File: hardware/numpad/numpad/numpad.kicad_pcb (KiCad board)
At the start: 4 copper layers, 123.8 x 142.9 mm, 57 parts, among them SW1 ROT_SKYLOONG_HS

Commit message: LEDs attached to switches
LEDs are assigned to the switches now
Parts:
- moved LED6 139.1 mm to (133.4, 71.1)
- moved LED5 136.4 mm to (133.5, 42.9)
- moved LED14 133.1 mm to (114.1, 91.1)
- moved LED8 120.0 mm to (95.3, 71.6)
- moved LED7 119.6 mm to (114.4, 71.9)
- moved LED4 117.6 mm to (114.4, 43.1)
- moved LED13 117.3 mm to (95.3, 90.6)
- moved LED12 103.0 mm to (76.3, 91.1)
- moved LED9 100.9 mm to (76.3, 71.8)
- moved LED3 99.4 mm to (95.4, 42.9)
- moved LED11 83.3 mm to (47.7, 90.8)
- moved LED2 81.7 mm to (76.3, 42.9)
- moved LED10 74.1 mm to (47.7, 71.8)
- moved LED1 56.6 mm to (47.6, 43.2)
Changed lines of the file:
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@@
 	(footprint "PCM_marbastlib-mx:LED_MX_6028R"
 		(layer "B.Cu")
-		(at -11.59 27.25 180)
+		(at 47.694 71.767 180)
 		(descr "Add-on for regular MX-footprints with 6028 reverse mount LED")
 		(tags "cherry MX 6028 rearmount rear mount led rgb backlight")
@@
 	(footprint "PCM_marbastlib-mx:LED_MX_6028R"
 		(layer "B.Cu")
-		(at -11.59 37.35 180)
+		(at 76.269 91.071 180)
 		(descr "Add-on for regular MX-footprints with 6028 reverse mount LED")
 		(tags "cherry MX 6028 rearmount rear mount led rgb backlight")
@@
 	(footprint "PCM_marbastlib-mx:LED_MX_6028R"
 		(layer "B.Cu")
-		(at -11.59 17.15 180)
+		(at 95.319 71.64 180)
 		(descr "Add-on for regular MX-footprints with 6028 reverse mount LED")
 		(tags "cherry MX 6028 rearmount rear mount led rgb backlight")
@@
 	(footprint "PCM_marbastlib-mx:LED_MX_6028R"
 		(layer "B.Cu")
-		(at -11.59 47.45 180)
+		(at 114.115 91.071 180)
 		(descr "Add-on for regular MX-footprints with 6028 reverse mount LED")
 		(tags "cherry MX 6028 rearmount rear mount led rgb backlight")
@@
 	(footprint "PCM_marbastlib-mx:LED_MX_6028R"
 		(layer "B.Cu")
-		(at -2.725 22.2 180)
+		(at 76.269 42.938 180)
 		(descr "Add-on for regular MX-footprints with 6028 reverse mount LED")
 		(tags "cherry MX 6028 rearmount rear mount led rgb backlight")
@@
 	(footprint "PCM_marbastlib-mx:LED_MX_6028R"
 		(layer "B.Cu")
-		(at -11.59 22.2 180)
+		(at 76.269 71.767 180)
 		(descr "Add-on for regular MX-footprints with 6028 reverse mount LED")
 		(tags "cherry MX 6028 rearmount rear mount led rgb backlight")
@@
 	(footprint "PCM_marbastlib-mx:LED_MX_6028R"
 		(layer "B.Cu")
-		(at -2.725 37.35 180)
+		(at 133.546 42.938 180)
 		(descr "Add-on for regular MX-footprints with 6028 reverse mount LED")
 		(tags "cherry MX 6028 rearmount rear mount led rgb backlight")
@@
 	(footprint "PCM_marbastlib-mx:LED_MX_6028R"
 		(layer "B.Cu")
-		(at -2.725 17.15 180)
+		(at 47.567 43.192 180)
 		(descr "Add-on for regular MX-footprints with 6028 reverse mount LED")
 		(tags "cherry MX 6028 rearmount rear mount led rgb backlight")
@@
 	(footprint "PCM_marbastlib-mx:LED_MX_6028R"
 		(layer "B.Cu")
-		(at -11.59 42.4 180)
+		(at 95.319 90.563 180)
 		(descr "Add-on for regular MX-footprints with 6028 reverse mount LED")
 		(tags "cherry MX 6028 rearmount rear mount led rgb backlight")
@@
 	(footprint "PCM_marbastlib-mx:LED_MX_6028R"
 		(layer "B.Cu")
-		(at -2.725 47.45 180)
+		(at 114.369 71.894 180)
 		(descr "Add-on for regular MX-footprints with 6028 reverse mount LED")
 		(tags "cherry MX 6028 rearmount rear mount led rgb backlight")
@@
 	(footprint "PCM_marbastlib-mx:LED_MX_6028R"
 		(layer "B.Cu")
-		(at -2.725 32.3 180)
+		(at 114.369 43.065 180)
 		(descr "Add-on for regular MX-footprints with 6028 reverse mount LED")
 		(tags "cherry MX 6028 rearmount rear mount led rgb backlight")
@@
 	(footprint "PCM_marbastlib-mx:LED_MX_6028R"
 		(layer "B.Cu")
-		(at -2.725 27.25 180)
+		(at 95.446 42.938 180)
 		(descr "Add-on for regular MX-footprints with 6028 reverse mount LED")
 		(tags "cherry MX 6028 rearmount rear mount led rgb backlight")
@@
 	(footprint "PCM_marbastlib-mx:LED_MX_6028R"
 		(layer "B.Cu")
-		(at -2.725 42.4 180)
+		(at 133.419 71.132 180)
 		(descr "Add-on for regular MX-footprints with 6028 reverse mount LED")
 		(tags "cherry MX 6028 rearmount rear mount led rgb backlight")
@@
 	(footprint "PCM_marbastlib-mx:LED_MX_6028R"
 		(layer "B.Cu")
-		(at -11.59 32.3 180)
+		(at 47.694 90.817 180)
 		(descr "Add-on for regular MX-footprints with 6028 reverse mount LED")
 		(tags "cherry MX 6028 rearmount rear mount led rgb backlight")

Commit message: led
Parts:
- moved LED27 178.0 mm to (142.8, -3.03)
- moved LED20 157.9 mm to (134.0, -3.03)
- moved LED25 154.2 mm to (142.8, 7.07)
- moved LED21 151.1 mm to (134.0, -8.08), turned to 0 degrees
- moved LED26 148.0 mm to (142.8, 2.02)
- moved LED19 137.7 mm to (134.0, 2.02)
- moved LED24 134.0 mm to (142.8, 12.1)
- moved LED23 120.9 mm to (142.8, 17.2)
- moved LED18 117.4 mm to (134.0, 7.07)
- moved LED11 114.0 mm to (125.1, 7.07), turned to 0 degrees
- moved LED22 109.9 mm to (142.8, 22.2)
- moved LED17 104.6 mm to (134.0, 12.1)
- moved LED12 101.6 mm to (125.1, 2.02), turned to 0 degrees
- moved LED14 99.8 mm to (125.1, -8.08), turned to 0 degrees
- moved LED13 98.2 mm to (125.1, -3.03), turned to 0 degrees
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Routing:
- net Net-(LED16-DOUT): track 48.2 -> 0.00 mm
- net Net-(LED1-DOUT): track 0.00 -> 43.3 mm
- net Net-(LED24-DOUT): track 39.1 -> 0.00 mm
- net Net-(LED1-DIN): track 0.00 -> 38.0 mm
- net Net-(LED25-DOUT): track 33.6 -> 0.00 mm
- net Net-(LED20-DIN): track 33.3 -> 0.00 mm
- net Net-(LED4-DIN): track 0.00 -> 28.9 mm
- net Net-(LED22-DOUT): track 28.6 -> 0.00 mm
- net Net-(LED23-DOUT): track 28.6 -> 0.00 mm
- net Net-(LED3-DIN): track 0.00 -> 28.6 mm
- net Net-(LED2-DIN): track 0.00 -> 28.6 mm
- net Net-(LED18-DIN): track 23.8 -> 0.00 mm
- net Net-(LED20-DOUT): track 23.7 -> 0.00 mm
- net Net-(LED21-DOUT): track 21.6 -> 0.00 mm
- net +5V: track 0.00 -> 19.2 mm, vias 0 -> 4
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
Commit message: pcb stuff
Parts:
- added C1: 20pF, PCM_Capacitor_SMD_AKL:C_0805_2012Metric, B.Cu at (84.6, 70.2)
- added C10: 1uF, PCM_Capacitor_SMD_AKL:C_0805_2012Metric, B.Cu at (73.3, 72.5)
- added C11: 0.1uF, PCM_Capacitor_SMD_AKL:C_0805_2012Metric, B.Cu at (89.6, 75.7)
- added C2: 20pF, PCM_Capacitor_SMD_AKL:C_0805_2012Metric, B.Cu at (84.6, 81.6)
- added C3: 100nF, PCM_Capacitor_SMD_AKL:C_0805_2012Metric, B.Cu at (67.7, 85.5)
- added C4: 100nF, PCM_Capacitor_SMD_AKL:C_0805_2012Metric, B.Cu at (60.0, 86.1)
- added C5: 100nF, PCM_Capacitor_SMD_AKL:C_0805_2012Metric, B.Cu at (57.4, 69.9)
- added C6: 100nF, PCM_Capacitor_SMD_AKL:C_0805_2012Metric, B.Cu at (68.1, 66.9)
- added C7: 1uF, PCM_Capacitor_SMD_AKL:C_0805_2012Metric, B.Cu at (74.6, 47.0)
- added C8: 10uF, PCM_Capacitor_SMD_AKL:C_0805_2012Metric, B.Cu at (83.8, 47.0)
- added C9: 4.7uF, PCM_Capacitor_SMD_AKL:C_0805_2012Metric, B.Cu at (62.3, 86.1)
- added D1: PRTR5V0U2X, PCM_Package_TO_SOT_SMD_AKL:SOT-143, B.Cu at (64.4, 56.0)
- added D10: 1N4148W, PCM_Diode_SMD_AKL:D_SOD-123, B.Cu at (175.7, 34.3)
- added D11: 1N4148W, PCM_Diode_SMD_AKL:D_SOD-123, B.Cu at (175.7, 38.4)
- added D12: 1N4148W, PCM_Diode_SMD_AKL:D_SOD-123, B.Cu at (175.7, 42.5)
- added D13: 1N4148W, PCM_Diode_SMD_AKL:D_SOD-123, B.Cu at (175.7, 46.6)
- added D14: 1N4148W, PCM_Diode_SMD_AKL:D_SOD-123, B.Cu at (175.7, 50.7)
- added D15: 1N4148W, PCM_Diode_SMD_AKL:D_SOD-123, B.Cu at (175.7, 54.8)
- added D16: 1N4148W, PCM_Diode_SMD_AKL:D_SOD-123, B.Cu at (175.7, 58.9)
- added D17: 1N4148W, PCM_Diode_SMD_AKL:D_SOD-123, B.Cu at (169.8, 34.3)
- added D18: 1N4148W, PCM_Diode_SMD_AKL:D_SOD-123, B.Cu at (169.8, 38.4)
- added D19: 1N4148W, PCM_Diode_SMD_AKL:D_SOD-123, B.Cu at (169.8, 42.5)
- added D2: BAT60JFILM, PCM_Diode_SMD_AKL:D_SOD-323, B.Cu at (71.3, 47.1)
- added D20: 1N4148W, PCM_Diode_SMD_AKL:D_SOD-123, B.Cu at (169.8, 46.6)
- added D21: 1N4148W, PCM_Diode_SMD_AKL:D_SOD-123, B.Cu at (169.8, 50.7)
- added D22: 1N4148W, PCM_Diode_SMD_AKL:D_SOD-123, B.Cu at (169.8, 54.8)
- added D23: 1N4148W, PCM_Diode_SMD_AKL:D_SOD-123, B.Cu at (169.8, 58.9)
- added D24: 1N4148W, PCM_Diode_SMD_AKL:D_SOD-123, B.Cu at (50.1, 99.7)
- added D25: 1N4148W, PCM_Diode_SMD_AKL:D_SOD-123, B.Cu at (50.2, 118.8)
- added D26: 1N4148W, PCM_Diode_SMD_AKL:D_SOD-123, B.Cu at (50.1, 137.8)
- added D27: 1N4148W, PCM_Diode_SMD_AKL:D_SOD-123, B.Cu at (50.1, 156.8)
- added D28: 1N4148W, PCM_Diode_SMD_AKL:D_SOD-123, B.Cu at (50.2, 175.9)
- added D29: 1N4148W, PCM_Diode_SMD_AKL:D_SOD-123, B.Cu at (41.1, 68.6)
- added D3: 1N4148W, PCM_Diode_SMD_AKL:D_SOD-123, B.Cu at (78.6, 71.1)
- added D4: 1N4148W, PCM_Diode_SMD_AKL:D_SOD-123, B.Cu at (181.6, 38.4)
- added D5: 1N4148W, PCM_Diode_SMD_AKL:D_SOD-123, B.Cu at (181.6, 42.5)
- added D6: 1N4148W, PCM_Diode_SMD_AKL:D_SOD-123, B.Cu at (181.6, 46.6)
- added D7: 1N4148W, PCM_Diode_SMD_AKL:D_SOD-123, B.Cu at (181.6, 50.7)
- added D8: 1N4148W, PCM_Diode_SMD_AKL:D_SOD-123, B.Cu at (181.6, 54.8)
- added D9: 1N4148W, PCM_Diode_SMD_AKL:D_SOD-123, B.Cu at (181.6, 58.9)
- added East1: Conn_01x04, Connector_PinSocket_2.54mm:PinSocket_1x04_P2.54mm_Vertical, F.Cu at (152.9, 110.2)
- added FB1: Ferrite_Bead, PCM_Fuse_AKL:Fuse_0805_2012Metric_Pad1.15x1.40mm_BigPads, B.Cu at (76.7, 79.3)
- added IC1: LD1117-3.3V-SOT223, PCM_4ms_Package_SOT:SOT223, B.Cu at (79.2, 47.0)
- added J1: Conn_01x06, Connector_PinSocket_2.54mm:PinSocket_1x06_P2.54mm_Horizontal, B.Cu at (43.9, 52.6)
- added North1: Conn_01x04, Connector_PinSocket_2.54mm:PinSocket_1x04_P2.54mm_Vertical, F.Cu at (89.2, 44.5)
- added R1: 5.1k, PCM_Resistor_SMD_AKL:R_0805_2012Metric, B.Cu at (68.7, 54.0)
- added R10: DNP, PCM_Resistor_SMD_AKL:R_0805_2012Metric, B.Cu at (73.3, 76.8)
- added R13: DNP, PCM_Resistor_SMD_AKL:R_0805_2012Metric, B.Cu at (104.0, 75.6)
- added R2: 5.1k, PCM_Resistor_SMD_AKL:R_0805_2012Metric, B.Cu at (60.3, 54.0)
- added R3: 22, PCM_Resistor_SMD_AKL:R_0805_2012Metric, B.Cu at (53.7, 75.4)
- added R4: 22, PCM_Resistor_SMD_AKL:R_0805_2012Metric, B.Cu at (53.7, 73.2)
- added R5: 10k, PCM_Resistor_SMD_AKL:R_0805_2012Metric, B.Cu at (65.8, 67.0)
- added R6: 22, PCM_Resistor_SMD_AKL:R_0805_2012Metric, B.Cu at (57.2, 64.1)
- added R7: 22, PCM_Resistor_SMD_AKL:R_0805_2012Metric, B.Cu at (53.7, 71.0)
- added R8: 22, PCM_Resistor_SMD_AKL:R_0805_2012Metric, B.Cu at (73.2, 70.2)
- added R9: 22, PCM_Resistor_SMD_AKL:R_0805_2012Metric, B.Cu at (63.5, 67.0)
- added SW2: Push_Button, PCM_marbastlib-various:SW_SPST_SKQG_WithStem, B.Cu at (97.7, 75.6)
- added South1: Conn_01x04, Connector_PinSocket_2.54mm:PinSocket_1x04_P2.54mm_Vertical, F.Cu at (96.8, 183.4)
- added U1: ~, footprints:LQFP64-10x10mm, B.Cu at (64.3, 76.2)
- added USB1: HRO-TYPE-C-31-M-12, Type-C.pretty-master:HRO-TYPE-C-31-M-12-HandSoldering, B.Cu at (64.4, 42.6)
- added West1: Conn_01x04, Connector_PinSocket_2.54mm:PinSocket_1x04_P2.54mm_Vertical, B.Cu at (33.1, 117.8)
- added Y1: 8MHz, PCM_Crystal_AKL:Crystal_HC52-U_Vertical, B.Cu at (84.6, 77.7)
- moved LED15 142.7 mm to (2.01, 76.5)
- moved LED16 142.7 mm to (2.01, 71.5)
- moved LED17 142.7 mm to (2.01, 66.4)
- moved LED18 142.7 mm to (2.01, 61.4)
- moved LED19 142.7 mm to (2.01, 56.3)
- moved LED20 142.7 mm to (2.01, 51.3)
- moved LED21 142.7 mm to (2.01, 46.2)
- moved LED6 142.7 mm to (-15.7, 51.3)
- moved LED7 142.7 mm to (-15.7, 46.2)
- moved LED11 142.7 mm to (-6.86, 61.4)
- moved LED12 142.7 mm to (-6.86, 56.3)
- moved LED13 142.7 mm to (-6.86, 51.3)
- moved LED14 142.7 mm to (-6.86, 46.2)
- moved LED22 142.7 mm to (10.9, 76.5)
- moved LED23 142.7 mm to (10.9, 71.5)
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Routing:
- net /UART_RX_SOUTH: track 0.00 -> 123.5 mm, vias 0 -> 1
- net /UART_TX_SOUTH: track 0.00 -> 122.4 mm, vias 0 -> 1
- net /UART_TX_EAST: track 0.00 -> 107.7 mm
- net /COL5: track 0.00 -> 107.3 mm, vias 0 -> 2
- net /UART_RX_EAST: track 0.00 -> 105.7 mm
- net /ROW6: track 0.00 -> 105.0 mm, vias 0 -> 2
- net /COL4: track 0.00 -> 89.7 mm, vias 0 -> 2
- net /ROW5: track 0.00 -> 86.0 mm, vias 0 -> 2
- net /COL3: track 0.00 -> 73.2 mm, vias 0 -> 2
- net /ROW4: track 0.00 -> 66.6 mm, vias 0 -> 2
- net +3.3V: track 0.00 -> 62.0 mm, vias 0 -> 3
- net /ROT_TIMA: track 0.00 -> 60.2 mm, vias 0 -> 1
- net /RGB_DATAIN: track 0.00 -> 58.2 mm, vias 0 -> 2
- net /COL2: track 0.00 -> 55.3 mm, vias 0 -> 2
- net /ROT_TIMB: track 0.00 -> 54.8 mm, vias 0 -> 1
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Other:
- board text added: "5VD"

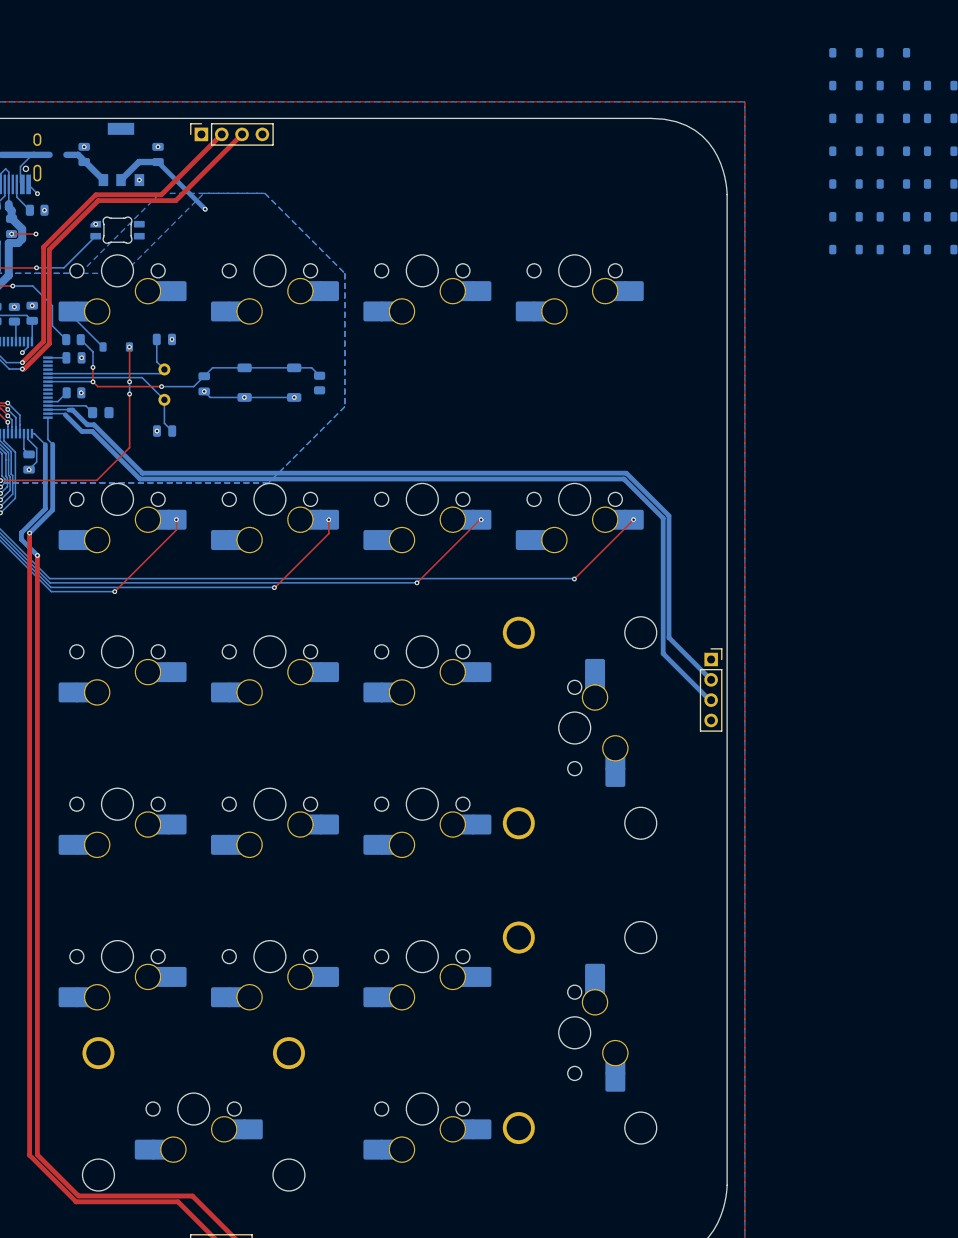
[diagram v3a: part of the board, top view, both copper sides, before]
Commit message: diodes placed except top 2 rows
🐷
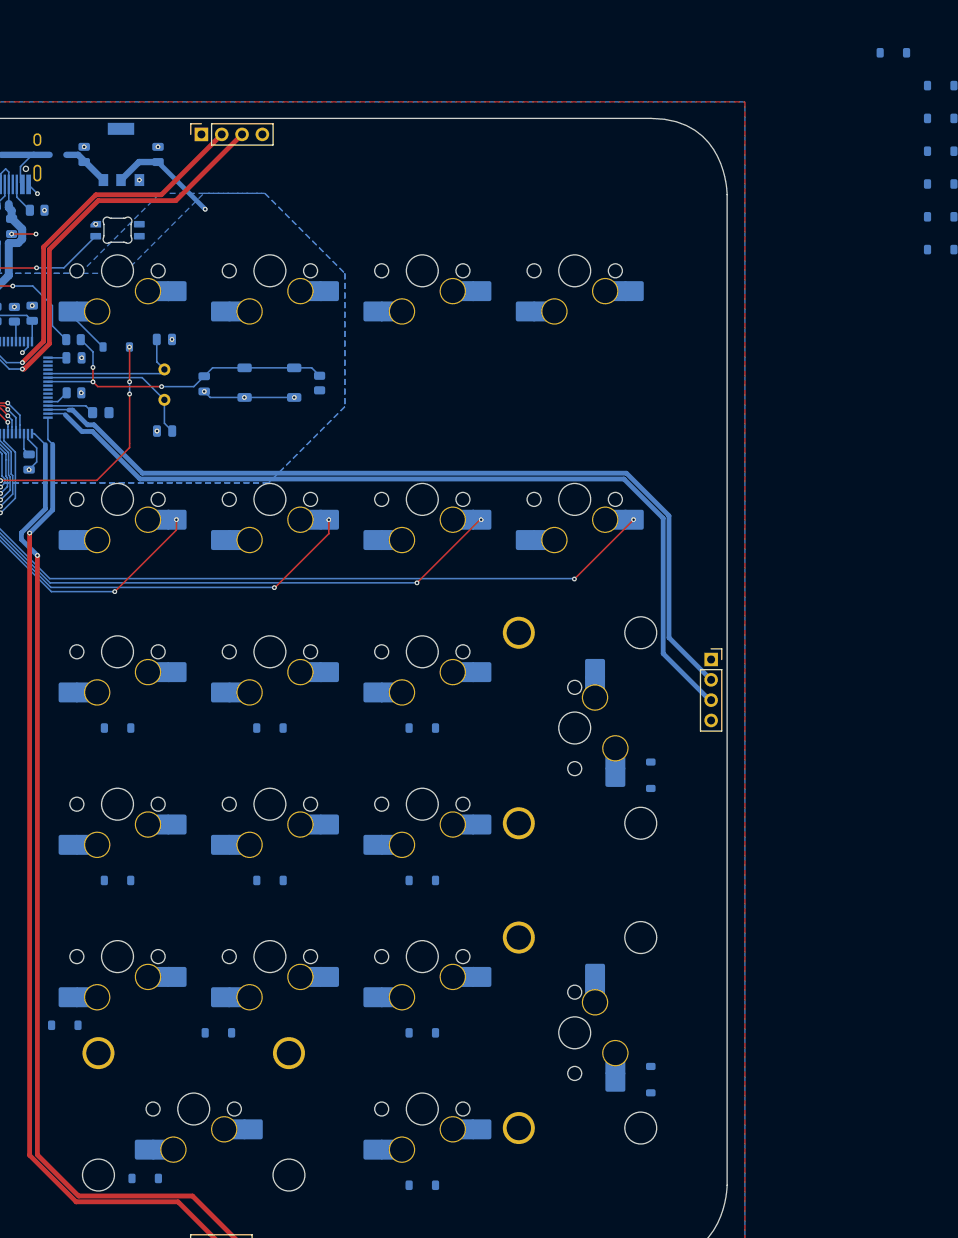
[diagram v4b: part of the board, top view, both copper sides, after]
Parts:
- moved D18 152.7 mm to (72.2, 155.9)
- moved D22 148.7 mm to (82.2, 175.1)
- moved D19 138.6 mm to (91.3, 156.8)
- moved D23 128.4 mm to (116.8, 175.9)
- moved D15 127.6 mm to (78.7, 137.8)
- moved D11 125.9 mm to (78.8, 118.8)
- moved D20 122.3 mm to (116.8, 156.8)
- moved D17 116.2 mm to (116.8, 137.8)
- moved D21 114.6 mm to (145.4, 162.7), turned to -90 degrees
- moved D16 110.9 mm to (97.8, 137.8)
- moved D12 109.0 mm to (97.8, 118.8)
- moved D13 93.1 mm to (116.8, 118.8)
- moved D14 79.9 mm to (145.4, 124.7), turned to -90 degrees
